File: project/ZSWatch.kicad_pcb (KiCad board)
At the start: 4 copper layers, 41 x 38 mm, 84 parts, among them IC1 nPM1300-QEXX, IC10 TS3USB221A, IC11 NTS0104GU12, IC12 DRV2603RUNT, IC2 APDS-9306-065, IC3 BMI270, IC4 BMP581, IC5 LIS2MDLTR, IC6 BME688, IC7 ESDALC6V1W5, IC8 FAN5622SX, IC9 S25FS512SAGNFI010, J1 CURRENT, M1 NORA-B106, Q1 BC817W, Q3 DMG1013UW-7, X1 BATTERY, X2 DOCK, X3 GC9A01A_CST816S, X4 M+, X5 M-

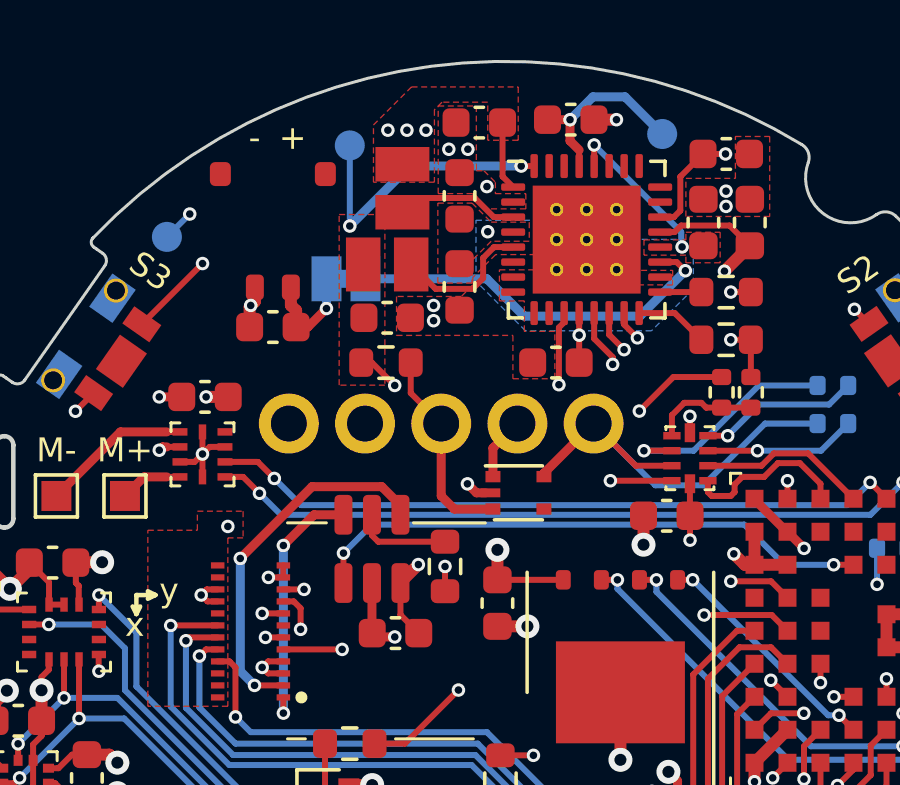
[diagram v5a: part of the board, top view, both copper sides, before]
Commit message: Update README, replace current measurement jumper with 0402 resistor on TOP side, update footprints and symbols
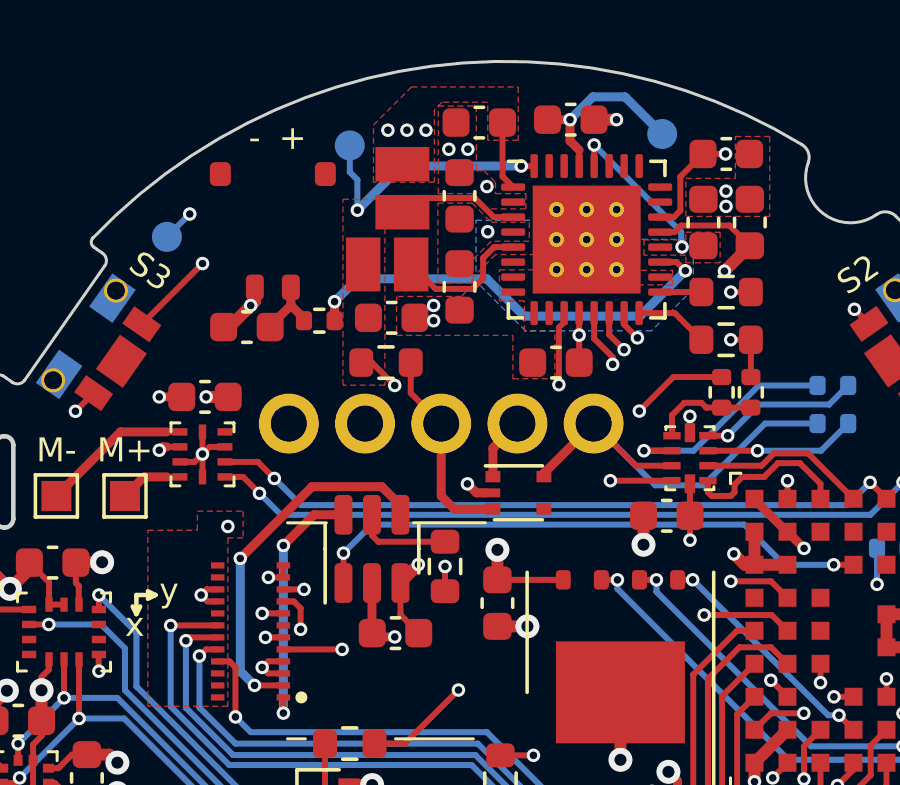
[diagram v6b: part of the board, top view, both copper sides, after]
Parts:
- removed J1: CURRENT, Jumper:SolderJumper-2_P1.3mm_Bridged_Pad1.0x1.5mm
- added R3: 0R, Resistor_SMD:R_0402_1005Metric, F.Cu at (153.2, 102.4)
- moved C3 0.87 mm to (150.7, 102.6)
- moved C5 0.15 mm to (155.6, 102.3)
- renumbered C12 to C11, C11 to C12, C23 to C14, C24 to C15, C14 to C16, C15 to C17, C16 to C18, C17 to C19, C18 to C20, C19 to C21, C20 to C22, C21 to C23, C22 to C24, Q3 to Q1, Q1 to Q2, R9 to R10, R10 to R11, R11 to R12, R12 to R13, R13 to R14, R7 to R15, R14 to R4, R3 to R5, R4 to R6, R5 to R7, R6 to R8, R8 to R9, TP2 to TP1, TP3 to TP2, TP1 to TP3
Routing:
- net Net-(IC1-VBAT): track 12.8 -> 14.7 mm, vias 1 -> 2
- net /Power Management/VBAT: track 3.66 -> 2.31 mm, vias 1 -> 0

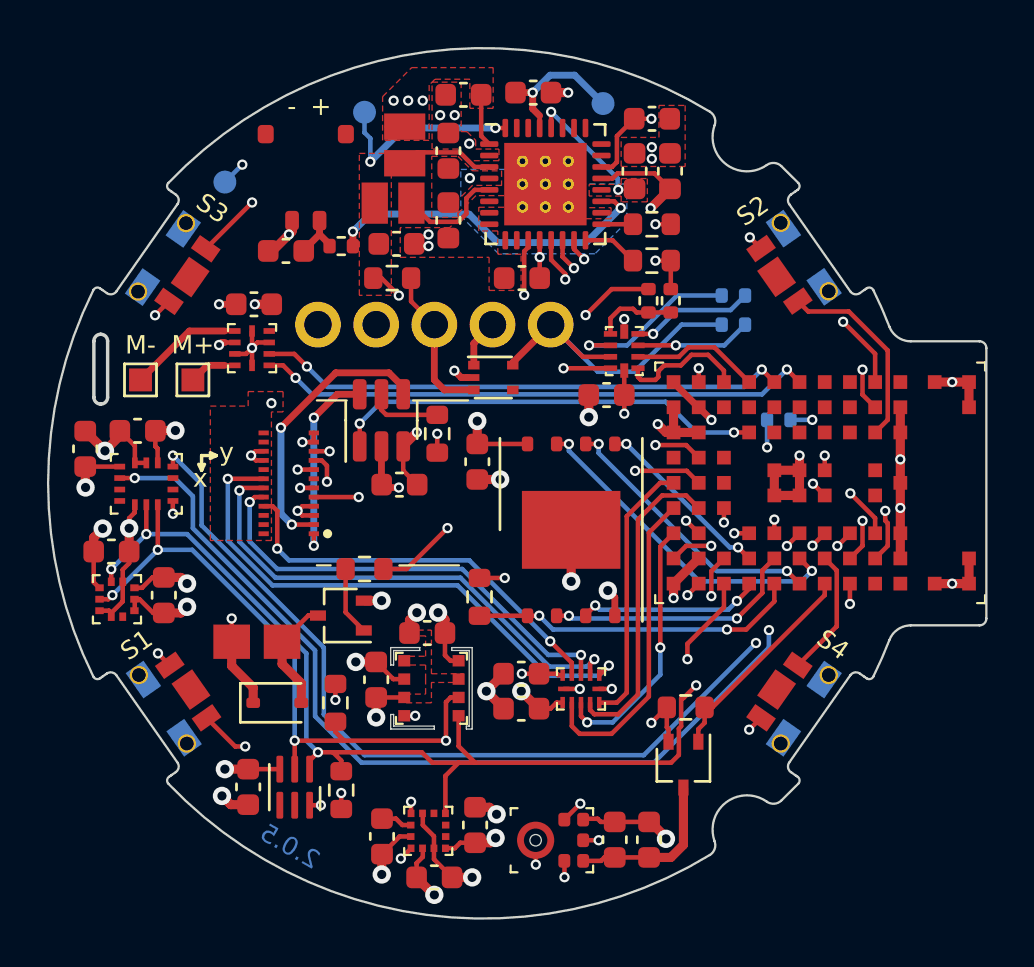
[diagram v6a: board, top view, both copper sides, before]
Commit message: Replace I2C mic with SPK0641HT4H-1
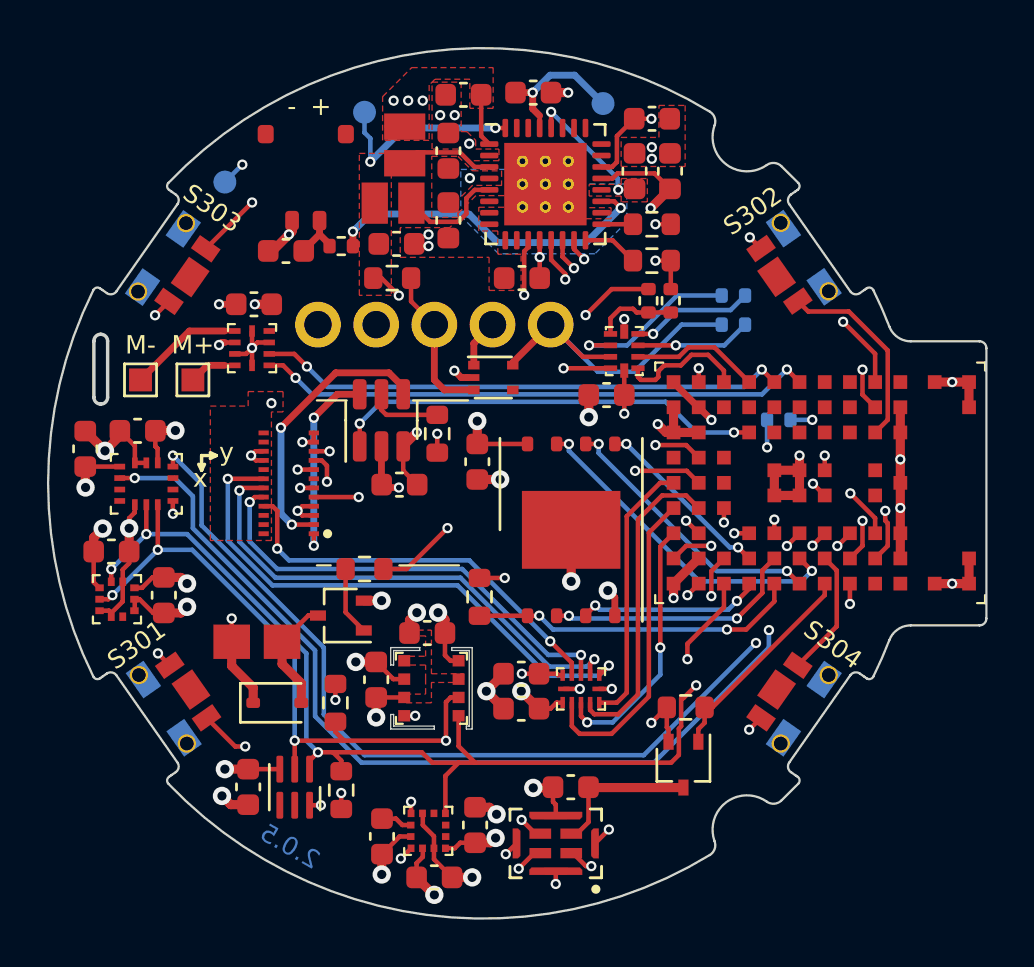
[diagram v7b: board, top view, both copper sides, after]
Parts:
- removed C14: 1u, Capacitor_SMD:C_0603_1608Metric
- removed C15: 200p, Capacitor_SMD:C_0603_1608Metric
- added C204: 100n, Capacitor_SMD:C_0603_1608Metric, F.Cu at (163.2, 126.0)
- MK201: renamed from MK1; footprint Knowles:SPH0645LM4H-6_3.5x2.65mm -> Knowles:SPK0641HT4H-1
- moved MK201 0.22 mm to (162.5, 128.4), turned to 90 degrees
- renumbered BZ1 to BZ301, C1 to C101, C2 to C102, C3 to C103, C4 to C104, C5 to C105, C6 to C106, C7 to C107, C8 to C108, C9 to C109, C10 to C110, C11 to C201, C12 to C202, C13 to C203, C16 to C206, C17 to C207, C18 to C208, C19 to C209, C20 to C210, C21 to C211, C22 to C212, C23 to C301, C24 to C302, C25 to C303, C26 to C304, C27 to C305, C28 to C306, D1 to D301, IC1 to IC101, IC2 to IC201, IC3 to IC202, IC4 to IC203, IC5 to IC204, IC6 to IC205, IC7 to IC301, IC8 to IC302, IC9 to IC303, IC10 to IC304, IC11 to IC305, IC12 to IC306, L1 to L101, L2 to L102, M1 to M301, Q1 to Q201, Q2 to Q301, R1 to R101, R2 to R102, R3 to R103, R4 to R201, R5 to R301, R6 to R302, R7 to R303, R8 to R304, R9 to R305, R10 to R306, R11 to R307, R12 to R308, R13 to R309, R14 to R310, R15 to R311, S1 to S301, S2 to S302, S3 to S303, S4 to S304, TP1 to TP101, TP2 to TP102, TP3 to TP103, X1 to X101, X2 to X301, X3 to X302, X4 to X303, X5 to X304
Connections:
- M301 pad F3: /MCU/MIC-DATA -> /MCU/MIC-CLK
- M301 pad G3: /MCU/MIC-BCLK -> /MCU/MIC-DATA
- MK201 pad 1: GND -> /MCU/MIC-DATA
- MK201 pad 2: /MCU/MIC-SEL -> /MCU/MIC-CLK
- MK201 pad 3: GND -> /MCU/MIC-SEL
- MK201 pad 4: /MCU/MIC-BCLK -> Net-(MK201-VDD)
- MK201 pad 5: Net-(MK1-VDD) -> GND
- MK201 pad 6: /MCU/MIC-DATA -> GND
- Q201 pad 3: Net-(MK1-VDD) -> Net-(MK201-VDD)
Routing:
- net /MCU/MIC-CLK: track 0.00 -> 22.9 mm, vias 0 -> 2
- net /MCU/MIC-BCLK: track 21.2 -> 0.00 mm, vias 2 -> 0
- net Net-(MK1-VDD): track 7.17 -> 0.00 mm
- net Net-(MK201-VDD): track 0.00 -> 6.64 mm
- net /MCU/MIC-SEL: track 19.4 -> 22.3 mm
- net /MCU/MIC-DATA: track 18.3 -> 20.2 mm
- net GND: track 78.7 -> 78.6 mm, vias 51 -> 53

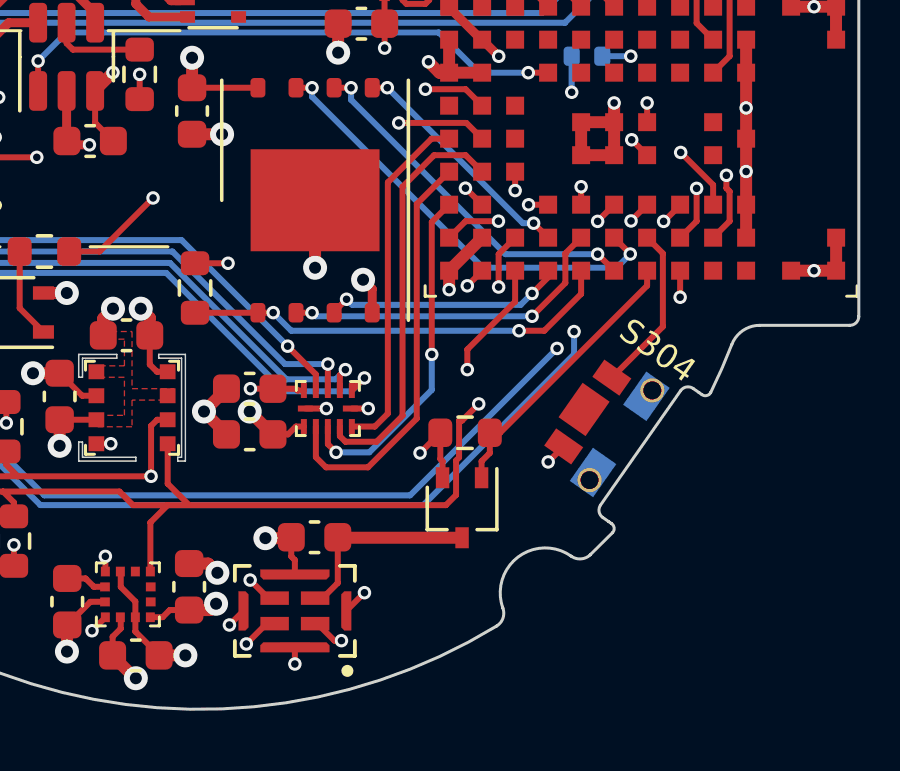
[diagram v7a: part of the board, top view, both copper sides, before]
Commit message: - Update mic footprint
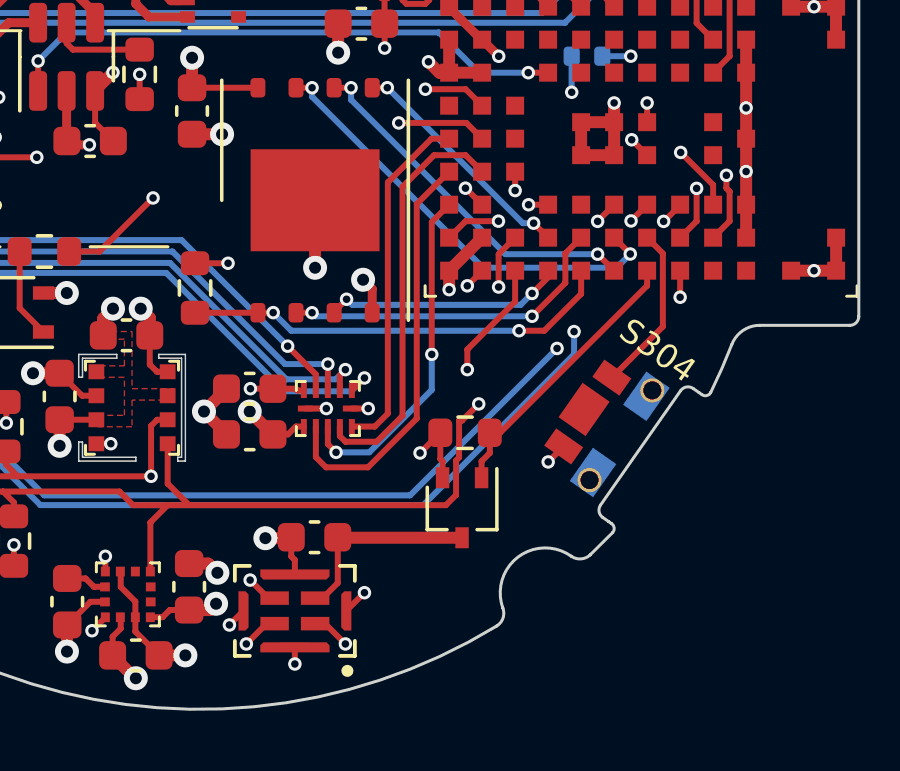
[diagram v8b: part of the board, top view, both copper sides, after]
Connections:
- M301 pad E3: /MCU/MIC-SEL -> unconnected-(M301B-P0.21-PadE3)
- MK201 pad 3: /MCU/MIC-SEL -> +1V8
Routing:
- net /MCU/MIC-SEL: track 22.3 -> 0.00 mm, vias 2 -> 0
- net +1V8: track 45.2 -> 46.2 mm, vias 22 -> 23
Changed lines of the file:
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@@
   (net 92 "unconnected-(M301C-P1.12-PadG8)")
   (net 93 "BUZZER")
-  (net 94 "/MCU/MIC-SEL")
+  (net 94 "unconnected-(M301B-P0.21-PadE3)")
   (net 95 "/MCU/MIC-DATA")
   (net 96 "unconnected-(M301C-P1.13-PadG9)")
@@
         (effects (font (size 1 1) (thickness 0.15)))
     )
-    (fp_text user "${REFERENCE}" (at -0.05 -0.05 180 unlocked) (layer "F.Fab")
+    (fp_text user "${REFERENCE}" (at -0.05 2.7 90 unlocked) (layer "F.Fab")
         (effects (font (size 0.8 0.8) (thickness 0.13)))
     )
@@
     (fp_circle (center -2 1.75) (end -1.9 1.75)
       (stroke (width 0.2) (type solid)) (fill none) (layer "F.Fab"))
+    (fp_circle (center 0 -0.97) (end 0.51 -0.97)
+      (stroke (width 0.1) (type default)) (fill none) (layer "F.Fab"))
     (pad "1" smd rect (at -0.425 0.675 90) (size 0.45 0.95) (layers "F.Cu" "F.Paste" "F.Mask")
       (net 95 "/MCU/MIC-DATA") (pinfunction "DATA") (pintype "output"))
@@
       (net 89 "/MCU/MIC-CLK") (pinfunction "CLK") (pintype "input"))
     (pad "3" smd rect (at 0.425 -0.675 90) (size 0.45 0.95) (layers "F.Cu" "F.Paste" "F.Mask")
-      (net 94 "/MCU/MIC-SEL") (pinfunction "SEL") (pintype "input"))
+      (net 3 "+1V8") (pinfunction "SEL") (pintype "input"))
     (pad "4" smd rect (at 0.425 0.675 90) (size 0.45 0.95) (layers "F.Cu" "F.Paste" "F.Mask")
       (net 28 "Net-(MK201-VDD)") (pinfunction "VDD") (pintype "power_in"))
@@
           (width 0.01) (fill yes))
       ))
+    (model "${KICAD_LIBRARY}/3D/Knowles/SPK0641HT4H.stp"
+      (offset (xyz 0 0 0))
+      (scale (xyz 1 1 1))
+      (rotate (xyz 90 180 180))
+    )
   )
   (footprint "Capacitor_SMD:C_0603_1608Metric" (layer "F.Cu")
@@
     (pad "33" thru_hole circle (at 1 1) (size 0.5 0.5) (drill 0.25) (layers "*.Cu")
       (net 2 "GND") (pinfunction "AVSS") (pintype "passive"))
-    (model "${KICAD6_3DMODEL_DIR}/Package_DFN_QFN.3dshapes/QFN-32-1EP_5x5mm_P0.5mm_EP3.6x3.6mm.wrl"
+    (model "${KICAD_LIBRARY}/3D/Packages/QFN-32-1EP_5x5mm_P0.5mm_EP3.6x3.6mm.step"
       (offset (xyz 0 0 0))
       (scale (xyz 1 1 1))
@@
     (pad "9" smd rect (at 0 0 90) (size 3.4 4.3) (layers "F.Cu" "F.Mask")
       (net 2 "GND") (pinfunction "EP") (pintype "passive"))
-    (model ":KICAD_LIBRARY:3D/Packages/WSON-8-8x6.stp"
+    (model "${KICAD_LIBRARY}/3D/Packages/WSON-8-8x6.stp"
       (offset (xyz 0 0 0))
       (scale (xyz 1 1 1))
@@
       (net 11 "QSPI-IO1") (pinfunction "P0.14/QSPI[1]") (pintype "bidirectional"))
     (pad "E3" smd rect (at -2.499996 2.099997 90) (size 0.6 0.6) (layers "F.Cu" "F.Paste" "F.Mask")
-      (net 94 "/MCU/MIC-SEL") (pinfunction "P0.21") (pintype "bidirectional"))
+      (net 94 "unconnected-(M301B-P0.21-PadE3)") (pinfunction "P0.21") (pintype "bidirectional+no_connect"))
     (pad "E4" smd rect (at -2.499998 0.449998 90) (size 0.6 0.6) (layers "F.Cu" "F.Paste" "F.Mask")
       (net 2 "GND") (pinfunction "GND") (pintype "power_in"))
@@
   (segment (start 145.145 111.826) (end 145.145 111.2015) (width 0.2) (layer "F.Cu") (net 3))
   (segment (start 149.098 125.1965) (end 150.48 125.1965) (width 0.2) (layer "F.Cu") (net 3))
+  (segment (start 161.638 128.013) (end 161.852 128.013) (width 0.2) (layer "F.Cu") (net 3))
   (segment (start 143.122 118.5415) (end 143.122 118.378) (width 0.2) (layer "F.Cu") (net 3))
   (segment (start 146.164 116.827) (end 145.415 116.827) (width 0.4) (layer "F.Cu") (net 3))
@@
   (segment (start 148.082 125.1965) (end 149.098 125.1965) (width 0.4) (layer "F.Cu") (net 3))
   (segment (start 159.271 97.55481) (end 159.271 95.758) (width 0.2) (layer "F.Cu") (net 3))
+  (segment (start 161.036 127.411) (end 161.638 128.013) (width 0.2) (layer "F.Cu") (net 3))
   (segment (start 155.25619 97.147) (end 155.93281 97.147) (width 0.4) (layer "F.Cu") (net 3))
   (segment (start 156.464 118.364) (end 156.140122 118.687878) (width 0.4) (layer "F.Cu") (net 3))
@@
   (via (at 148.844 98.806) (size 0.45) (drill 0.25) (layers "F.Cu" "B.Cu") (net 3))
   (via (at 159.9 128.2) (size 0.8) (drill 0.4) (layers "F.Cu" "B.Cu") (net 3))
+  (via (at 161.036 127.411) (size 0.45) (drill 0.25) (layers "F.Cu" "B.Cu") (net 3))
   (via (at 148.082 125.1965) (size 0.8) (drill 0.4) (layers "F.Cu" "B.Cu") (net 3))
   (via (at 142 112.9) (size 0.8) (drill 0.4) (layers "F.Cu" "B.Cu") (net 3))
@@
   (segment (start 157.8 114.673299) (end 165.488701 114.673299) (width 0.2) (layer "In2.Cu") (net 93))
   (segment (start 165.488701 114.673299) (end 166.878 113.284) (width 0.2) (layer "In2.Cu") (net 93))
-  (segment (start 172.068602 114.3) (end 172.068602 114.897799) (width 0.2) (layer "F.Cu") (net 94))
-  (segment (start 161.638 128.013) (end 161.852 128.013) (width 0.2) (layer "F.Cu") (net 94))
-  (segment (start 161.036 127.411) (end 161.638 128.013) (width 0.2) (layer "F.Cu") (net 94))
-  (via (at 172.068602 114.3) (size 0.45) (drill 0.25) (layers "F.Cu" "B.Cu") (net 94))
-  (via (at 161.036 127.411) (size 0.45) (drill 0.25) (layers "F.Cu" "B.Cu") (net 94))
-  (segment (start 172.8 119.681) (end 172.8 117.555) (width 0.2) (layer "In1.Cu") (net 94))
-  (segment (start 172.068602 116.823602) (end 172.068602 114.3) (width 0.2) (layer "In1.Cu") (net 94))
-  (segment (start 172.8 117.555) (end 172.068602 116.823602) (width 0.2) (layer "In1.Cu") (net 94))
-  (segment (start 166.116 126.365) (end 172.8 119.681) (width 0.2) (layer "In1.Cu") (net 94))
-  (segment (start 162.082 126.365) (end 166.116 126.365) (width 0.2) (layer "In1.Cu") (net 94))
-  (segment (start 161.036 127.411) (end 162.082 126.365) (width 0.2) (layer "In1.Cu") (net 94))
   (segment (start 173.732966 115.439677) (end 173.732966 115.433435) (width 0.2) (layer "F.Cu") (net 95))
-  (segment (start 164.079166 129.429461) (end 163.844313 129.429461) (width 0.2) (layer "F.Cu") (net 95))
-  (segment (start 163.844313 129.429461) (end 163.277852 128.863) (width 0.2) (layer "F.Cu") (net 95))
   (segment (start 173.732966 115.433435) (end 174.268602 114.897799) (width 0.2) (layer "F.Cu") (net 95))
-  (segment (start 163.277852 128.863) (end 163.202 128.863) (width 0.2) (layer "F.Cu") (net 95))
-  (via (at 164.079166 129.429461) (size 0.45) (drill 0.25) (layers "F.Cu" "B.Cu") (net 95))
+  (segment (start 164.211 129.54) (end 163.534 128.863) (width 0.2) (layer "F.Cu") (net 95))
+  (segment (start 163.534 128.863) (end 163.202 128.863) (width 0.2) (layer "F.Cu") (net 95))
+  (via (at 164.211 129.54) (size 0.45) (drill 0.25) (layers "F.Cu" "B.Cu") (net 95))
   (via (at 173.732966 115.439677) (size 0.45) (drill 0.25) (layers "F.Cu" "B.Cu") (net 95))
-  (segment (start 164.082659 129.429461) (end 173.55012 119.962) (width 0.2) (layer "In1.Cu") (net 95))
-  (segment (start 164.079166 129.429461) (end 164.082659 129.429461) (width 0.2) (layer "In1.Cu") (net 95))
-  (segment (start 173.55012 117.507018) (end 174.157138 116.9) (width 0.2) (layer "In1.Cu") (net 95))
-  (segment (start 174.157138 116.9) (end 174.157138 115.863849) (width 0.2) (layer "In1.Cu") (net 95))
+  (segment (start 164.211 129.54) (end 173.55012 120.20088) (width 0.2) (layer "In1.Cu") (net 95))
   (segment (start 174.157138 115.863849) (end 173.732966 115.439677) (width 0.2) (layer "In1.Cu") (net 95))
-  (segment (start 173.55012 119.962) (end 173.55012 117.507018) (width 0.2) (layer "In1.Cu") (net 95))
+  (segment (start 174.157138 116.9) (end 174.157138 115.863849) (width 0.2) (layer "In1.Cu") (net 95))
+  (segment (start 173.55012 117.507018) (end 174.157138 116.9) (width 0.2) (layer "In1.Cu") (net 95))
+  (segment (start 173.55012 120.20088) (end 173.55012 117.507018) (width 0.2) (layer "In1.Cu") (net 95))
   (segment (start 159.766 105.791) (end 158.95 106.607) (width 0.3) (layer "F.Cu") (net 97))
   (segment (start 163.9824 106.696) (end 164.916 106.696) (width 0.2) (layer "F.Cu") (net 97))
